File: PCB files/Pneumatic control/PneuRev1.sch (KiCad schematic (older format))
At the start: 52 parts, among them J1 SIG_IN, J2 BATT_IN, J3 PNEU, U1 uA7824, U2 OP279, U3 OP279, U4 OP279, U5 OP279, U6 OP279, U7 OP279, U8 OP07

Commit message: 2/4/2019
-Finished board routing
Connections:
- net at U1.3 (OUT), U2.8 (V+), U3.8 (V+)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: now also U2.8 (V+), U3.8 (V+), U4.8 (V+), U4.8 (V+), U5.8 (V+), U6.8 (V+), U7.8 (V+), U7.8 (V+)
- no-connect marks 24 -> 22
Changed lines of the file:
@@
 EESchema Schematic File Version 2
+LIBS:PneuRev1-rescue
 LIBS:power
 LIBS:device
@@
 	1    0    0    -1
 $EndComp
-NoConn ~ 4625 1800
-NoConn ~ 4725 1800
 Wire Wire Line
 	4925 1500 5325 1500
@@
 	1950 875  1900 875
 $Comp
-L GND #PWR?
+L GND #PWR041
 U 1 1 5C53AC5E
 P 2350 1100
-F 0 "#PWR?" H 2350 850 50  0001 C CNN
+F 0 "#PWR041" H 2350 850 50  0001 C CNN
 F 1 "GND" H 2350 950 50  0000 C CNN
 F 2 "" H 2350 1100 50  0001 C CNN
@@
 $EndComp
 Connection ~ 2350 1025
+Wire Wire Line
+	3675 1200 3675 4325
+Connection ~ 3675 1200
+Connection ~ 3675 2775
+Connection ~ 3675 4325
 $EndSCHEMATC

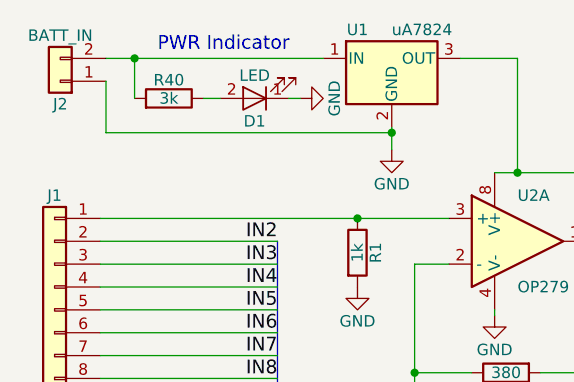
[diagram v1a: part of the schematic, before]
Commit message: 2/10/2019
-Changed LED resistor to 1.5k
-Set BATT connector to a JST
-Found 383 ohm resistor to replace 390 ohm
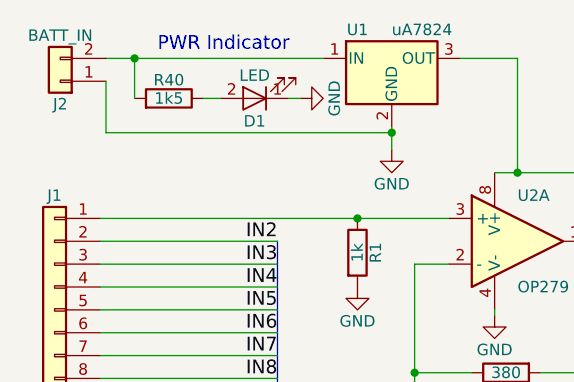
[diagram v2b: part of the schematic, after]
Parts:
- J2: footprint Connectors_Molex:Molex_KK-6410-02_02x2.54mm_Straight -> Connectors_JST:JST_XH_B02B-XH-A_02x2.50mm_Straight
- R40: value 3k -> 1k5; footprint Resistors_THT:R_Axial_DIN0204_L3.6mm_D1.6mm_P5.08mm_Horizontal -> Resistors_THT:R_Axial_DIN0411_L9.9mm_D3.6mm_P15.24mm_Horizontal
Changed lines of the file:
@@
 F 0 "J2" H 900 900 50  0000 C CNN
 F 1 "BATT_IN" H 900 600 50  0000 C CNN
-F 2 "Connectors_Molex:Molex_KK-6410-02_02x2.54mm_Straight" H 900 800 50  0001 C CNN
+F 2 "Connectors_JST:JST_XH_B02B-XH-A_02x2.50mm_Straight" H 900 800 50  0001 C CNN
 F 3 "" H 900 800 50  0001 C CNN
 	1    900  800
@@
 P 1375 875
 F 0 "R40" V 1455 875 50  0000 C CNN
-F 1 "3k" V 1375 875 50  0000 C CNN
-F 2 "Resistors_THT:R_Axial_DIN0204_L3.6mm_D1.6mm_P5.08mm_Horizontal" V 1305 875 50  0001 C CNN
+F 1 "1k5" V 1375 875 50  0000 C CNN
+F 2 "Resistors_THT:R_Axial_DIN0411_L9.9mm_D3.6mm_P15.24mm_Horizontal" V 1305 875 50  0001 C CNN
 F 3 "" H 1375 875 50  0001 C CNN
 	1    1375 875

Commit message: 2/12/2019
-Footprint updates
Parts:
- R13, R14, R15, R22, R23, R24, R31, R32, R33, R38, R4, R5, R6: footprint Resistors_THT:R_Axial_DIN0204_L3.6mm_D1.6mm_P5.08mm_Horizontal -> Resistors_THT:R_Axial_DIN0204_L3.6mm_D1.6mm_P7.62mm_Horizontal
- R16, R17, R18, R25, R26, R27, R34, R35, R36, R39: value 380 -> 400; footprint Resistors_THT:R_Axial_DIN0204_L3.6mm_D1.6mm_P5.08mm_Horizontal -> Resistors_THT:R_Axial_DIN0411_L9.9mm_D3.6mm_P12.70mm_Horizontal
- R7, R8, R9: value 380 -> 400; footprint Resistors_THT:R_Axial_DIN0204_L3.6mm_D1.6mm_P5.08mm_Horizontal -> Resistors_THT:R_Axial_DIN0309_L9.0mm_D3.2mm_P12.70mm_Horizontal
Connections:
- no-connect marks 22 -> 14
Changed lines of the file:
@@
 F 0 "R4" V 2530 2300 50  0000 C CNN
 F 1 "100" V 2450 2300 50  0000 C CNN
-F 2 "Resistors_THT:R_Axial_DIN0204_L3.6mm_D1.6mm_P5.08mm_Horizontal" V 2380 2300 50  0001 C CNN
+F 2 "Resistors_THT:R_Axial_DIN0204_L3.6mm_D1.6mm_P7.62mm_Horizontal" V 2400 2300 50  0001 C CNN
 F 3 "" H 2450 2300 50  0001 C CNN
 	1    2450 2300
@@
 P 2850 2075
 F 0 "R7" V 2930 2075 50  0000 C CNN
-F 1 "380" V 2850 2075 50  0000 C CNN
-F 2 "Resistors_THT:R_Axial_DIN0204_L3.6mm_D1.6mm_P5.08mm_Horizontal" V 2780 2075 50  0001 C CNN
+F 1 "400" V 2850 2075 50  0000 C CNN
+F 2 "Resistors_THT:R_Axial_DIN0309_L9.0mm_D3.2mm_P12.70mm_Horizontal" V 2780 2075 50  0001 C CNN
 F 3 "" H 2850 2075 50  0001 C CNN
 	1    2850 2075
@@
 F 0 "R5" V 2530 3875 50  0000 C CNN
 F 1 "100" V 2450 3875 50  0000 C CNN
-F 2 "Resistors_THT:R_Axial_DIN0204_L3.6mm_D1.6mm_P5.08mm_Horizontal" V 2380 3875 50  0001 C CNN
+F 2 "Resistors_THT:R_Axial_DIN0204_L3.6mm_D1.6mm_P7.62mm_Horizontal" V 2400 3875 50  0001 C CNN
 F 3 "" H 2450 3875 50  0001 C CNN
 	1    2450 3875
@@
 P 2850 3650
 F 0 "R8" V 2930 3650 50  0000 C CNN
-F 1 "380" V 2850 3650 50  0000 C CNN
-F 2 "Resistors_THT:R_Axial_DIN0204_L3.6mm_D1.6mm_P5.08mm_Horizontal" V 2780 3650 50  0001 C CNN
+F 1 "400" V 2850 3650 50  0000 C CNN
+F 2 "Resistors_THT:R_Axial_DIN0309_L9.0mm_D3.2mm_P12.70mm_Horizontal" V 2780 3650 50  0001 C CNN
 F 3 "" H 2850 3650 50  0001 C CNN
 	1    2850 3650
@@
 F 0 "R6" V 2580 5425 50  0000 C CNN
 F 1 "100" V 2500 5425 50  0000 C CNN
-F 2 "Resistors_THT:R_Axial_DIN0204_L3.6mm_D1.6mm_P5.08mm_Horizontal" V 2430 5425 50  0001 C CNN
+F 2 "Resistors_THT:R_Axial_DIN0204_L3.6mm_D1.6mm_P7.62mm_Horizontal" V 2430 5425 50  0001 C CNN
 F 3 "" H 2500 5425 50  0001 C CNN
 	1    2500 5425
@@
 P 2900 5200
 F 0 "R9" V 2980 5200 50  0000 C CNN
-F 1 "380" V 2900 5200 50  0000 C CNN
-F 2 "Resistors_THT:R_Axial_DIN0204_L3.6mm_D1.6mm_P5.08mm_Horizontal" V 2830 5200 50  0001 C CNN
+F 1 "400" V 2900 5200 50  0000 C CNN
+F 2 "Resistors_THT:R_Axial_DIN0309_L9.0mm_D3.2mm_P12.70mm_Horizontal" V 2830 5200 50  0001 C CNN
 F 3 "" H 2900 5200 50  0001 C CNN
 	1    2900 5200
@@
 F 0 "R13" V 4255 2300 50  0000 C CNN
 F 1 "100" V 4175 2300 50  0000 C CNN
-F 2 "Resistors_THT:R_Axial_DIN0204_L3.6mm_D1.6mm_P5.08mm_Horizontal" V 4105 2300 50  0001 C CNN
+F 2 "Resistors_THT:R_Axial_DIN0204_L3.6mm_D1.6mm_P7.62mm_Horizontal" V 4105 2300 50  0001 C CNN
 F 3 "" H 4175 2300 50  0001 C CNN
 	1    4175 2300
@@
 P 4575 2075
 F 0 "R16" V 4655 2075 50  0000 C CNN
-F 1 "380" V 4575 2075 50  0000 C CNN
-F 2 "Resistors_THT:R_Axial_DIN0204_L3.6mm_D1.6mm_P5.08mm_Horizontal" V 4505 2075 50  0001 C CNN
+F 1 "400" V 4575 2075 50  0000 C CNN
+F 2 "Resistors_THT:R_Axial_DIN0411_L9.9mm_D3.6mm_P12.70mm_Horizontal" V 4505 2075 50  0001 C CNN
 F 3 "" H 4575 2075 50  0001 C CNN
 	1    4575 2075
@@
 F 0 "R14" V 4255 3875 50  0000 C CNN
 F 1 "100" V 4175 3875 50  0000 C CNN
-F 2 "Resistors_THT:R_Axial_DIN0204_L3.6mm_D1.6mm_P5.08mm_Horizontal" V 4105 3875 50  0001 C CNN
+F 2 "Resistors_THT:R_Axial_DIN0204_L3.6mm_D1.6mm_P7.62mm_Horizontal" V 4105 3875 50  0001 C CNN
 F 3 "" H 4175 3875 50  0001 C CNN
 	1    4175 3875
@@
 P 4575 3650
 F 0 "R17" V 4655 3650 50  0000 C CNN
-F 1 "380" V 4575 3650 50  0000 C CNN
-F 2 "Resistors_THT:R_Axial_DIN0204_L3.6mm_D1.6mm_P5.08mm_Horizontal" V 4505 3650 50  0001 C CNN
+F 1 "400" V 4575 3650 50  0000 C CNN
+F 2 "Resistors_THT:R_Axial_DIN0411_L9.9mm_D3.6mm_P12.70mm_Horizontal" V 4505 3650 50  0001 C CNN
 F 3 "" H 4575 3650 50  0001 C CNN
 	1    4575 3650
@@
 F 0 "R15" V 4305 5425 50  0000 C CNN
 F 1 "100" V 4225 5425 50  0000 C CNN
-F 2 "Resistors_THT:R_Axial_DIN0204_L3.6mm_D1.6mm_P5.08mm_Horizontal" V 4155 5425 50  0001 C CNN
+F 2 "Resistors_THT:R_Axial_DIN0204_L3.6mm_D1.6mm_P7.62mm_Horizontal" V 4155 5425 50  0001 C CNN
 F 3 "" H 4225 5425 50  0001 C CNN
 	1    4225 5425
@@
 P 4625 5200
 F 0 "R18" V 4705 5200 50  0000 C CNN
-F 1 "380" V 4625 5200 50  0000 C CNN
-F 2 "Resistors_THT:R_Axial_DIN0204_L3.6mm_D1.6mm_P5.08mm_Horizontal" V 4555 5200 50  0001 C CNN
+F 1 "400" V 4625 5200 50  0000 C CNN
+F 2 "Resistors_THT:R_Axial_DIN0411_L9.9mm_D3.6mm_P12.70mm_Horizontal" V 4555 5200 50  0001 C CNN
 F 3 "" H 4625 5200 50  0001 C CNN
 	1    4625 5200
@@
 F 0 "R22" V 5830 2300 50  0000 C CNN
 F 1 "100" V 5750 2300 50  0000 C CNN
-F 2 "Resistors_THT:R_Axial_DIN0204_L3.6mm_D1.6mm_P5.08mm_Horizontal" V 5680 2300 50  0001 C CNN
+F 2 "Resistors_THT:R_Axial_DIN0204_L3.6mm_D1.6mm_P7.62mm_Horizontal" V 5680 2300 50  0001 C CNN
 F 3 "" H 5750 2300 50  0001 C CNN
 	1    5750 2300
@@
 P 6150 2075
 F 0 "R25" V 6230 2075 50  0000 C CNN
-F 1 "380" V 6150 2075 50  0000 C CNN
-F 2 "Resistors_THT:R_Axial_DIN0204_L3.6mm_D1.6mm_P5.08mm_Horizontal" V 6080 2075 50  0001 C CNN
+F 1 "400" V 6150 2075 50  0000 C CNN
+F 2 "Resistors_THT:R_Axial_DIN0411_L9.9mm_D3.6mm_P12.70mm_Horizontal" V 6080 2075 50  0001 C CNN
 F 3 "" H 6150 2075 50  0001 C CNN
 	1    6150 2075
@@
 	1    0    0    -1
 $EndComp
-NoConn ~ 6200 1800
-NoConn ~ 6300 1800
 Wire Wire Line
 	6500 1500 7000 1500
@@
 F 0 "R23" V 5830 3875 50  0000 C CNN
 F 1 "100" V 5750 3875 50  0000 C CNN
-F 2 "Resistors_THT:R_Axial_DIN0204_L3.6mm_D1.6mm_P5.08mm_Horizontal" V 5680 3875 50  0001 C CNN
+F 2 "Resistors_THT:R_Axial_DIN0204_L3.6mm_D1.6mm_P7.62mm_Horizontal" V 5680 3875 50  0001 C CNN
 F 3 "" H 5750 3875 50  0001 C CNN
 	1    5750 3875
@@
 P 6150 3650
 F 0 "R26" V 6230 3650 50  0000 C CNN
-F 1 "380" V 6150 3650 50  0000 C CNN
-F 2 "Resistors_THT:R_Axial_DIN0204_L3.6mm_D1.6mm_P5.08mm_Horizontal" V 6080 3650 50  0001 C CNN
+F 1 "400" V 6150 3650 50  0000 C CNN
+F 2 "Resistors_THT:R_Axial_DIN0411_L9.9mm_D3.6mm_P12.70mm_Horizontal" V 6080 3650 50  0001 C CNN
 F 3 "" H 6150 3650 50  0001 C CNN
 	1    6150 3650
@@
 	1    0    0    -1
 $EndComp
-NoConn ~ 6200 3375
-NoConn ~ 6300 3375
 Wire Wire Line
 	6500 3075 7000 3075
@@
 F 0 "R24" V 5880 5425 50  0000 C CNN
 F 1 "100" V 5800 5425 50  0000 C CNN
-F 2 "Resistors_THT:R_Axial_DIN0204_L3.6mm_D1.6mm_P5.08mm_Horizontal" V 5730 5425 50  0001 C CNN
+F 2 "Resistors_THT:R_Axial_DIN0204_L3.6mm_D1.6mm_P7.62mm_Horizontal" V 5730 5425 50  0001 C CNN
 F 3 "" H 5800 5425 50  0001 C CNN
 	1    5800 5425
@@
 P 6200 5200
 F 0 "R27" V 6280 5200 50  0000 C CNN
-F 1 "380" V 6200 5200 50  0000 C CNN
-F 2 "Resistors_THT:R_Axial_DIN0204_L3.6mm_D1.6mm_P5.08mm_Horizontal" V 6130 5200 50  0001 C CNN
+F 1 "400" V 6200 5200 50  0000 C CNN
+F 2 "Resistors_THT:R_Axial_DIN0411_L9.9mm_D3.6mm_P12.70mm_Horizontal" V 6130 5200 50  0001 C CNN
 F 3 "" H 6200 5200 50  0001 C CNN
 	1    6200 5200
@@
 F 0 "R31" V 7580 2300 50  0000 C CNN
 F 1 "100" V 7500 2300 50  0000 C CNN
-F 2 "Resistors_THT:R_Axial_DIN0204_L3.6mm_D1.6mm_P5.08mm_Horizontal" V 7430 2300 50  0001 C CNN
+F 2 "Resistors_THT:R_Axial_DIN0204_L3.6mm_D1.6mm_P7.62mm_Horizontal" V 7430 2300 50  0001 C CNN
 F 3 "" H 7500 2300 50  0001 C CNN
 	1    7500 2300
@@
 P 7900 2075
 F 0 "R34" V 7980 2075 50  0000 C CNN
-F 1 "380" V 7900 2075 50  0000 C CNN
-F 2 "Resistors_THT:R_Axial_DIN0204_L3.6mm_D1.6mm_P5.08mm_Horizontal" V 7830 2075 50  0001 C CNN
+F 1 "400" V 7900 2075 50  0000 C CNN
+F 2 "Resistors_THT:R_Axial_DIN0411_L9.9mm_D3.6mm_P12.70mm_Horizontal" V 7830 2075 50  0001 C CNN
 F 3 "" H 7900 2075 50  0001 C CNN
 	1    7900 2075
@@
 	1    0    0    -1
 $EndComp
-NoConn ~ 7950 1800
-NoConn ~ 8050 1800
 Wire Wire Line
 	8250 1500 8675 1500
@@
 F 0 "R32" V 7580 3875 50  0000 C CNN
 F 1 "100" V 7500 3875 50  0000 C CNN
-F 2 "Resistors_THT:R_Axial_DIN0204_L3.6mm_D1.6mm_P5.08mm_Horizontal" V 7430 3875 50  0001 C CNN
+F 2 "Resistors_THT:R_Axial_DIN0204_L3.6mm_D1.6mm_P7.62mm_Horizontal" V 7430 3875 50  0001 C CNN
 F 3 "" H 7500 3875 50  0001 C CNN
 	1    7500 3875
@@
 P 7900 3650
 F 0 "R35" V 7980 3650 50  0000 C CNN
-F 1 "380" V 7900 3650 50  0000 C CNN
-F 2 "Resistors_THT:R_Axial_DIN0204_L3.6mm_D1.6mm_P5.08mm_Horizontal" V 7830 3650 50  0001 C CNN
+F 1 "400" V 7900 3650 50  0000 C CNN
+F 2 "Resistors_THT:R_Axial_DIN0411_L9.9mm_D3.6mm_P12.70mm_Horizontal" V 7830 3650 50  0001 C CNN
 F 3 "" H 7900 3650 50  0001 C CNN
 	1    7900 3650
@@
 	1    0    0    -1
 $EndComp
-NoConn ~ 7950 3375
-NoConn ~ 8050 3375
 Wire Wire Line
 	8250 3075 8675 3075
@@
 U 1 1 5C023441
 P 7300 4675
-F 0 "R30" V 7380 4675 50  0000 C CNN
+F 0 "R30" V 7400 4675 50  0000 C CNN
 F 1 "1k" V 7300 4675 50  0000 C CNN
 F 2 "Resistors_THT:R_Axial_DIN0204_L3.6mm_D1.6mm_P5.08mm_Horizontal" V 7230 4675 50  0001 C CNN
@@
 F 0 "R33" V 7630 5425 50  0000 C CNN
 F 1 "100" V 7550 5425 50  0000 C CNN
-F 2 "Resistors_THT:R_Axial_DIN0204_L3.6mm_D1.6mm_P5.08mm_Horizontal" V 7480 5425 50  0001 C CNN
+F 2 "Resistors_THT:R_Axial_DIN0204_L3.6mm_D1.6mm_P7.62mm_Horizontal" V 7480 5425 50  0001 C CNN
 F 3 "" H 7550 5425 50  0001 C CNN
 	1    7550 5425
@@
 P 7950 5200
 F 0 "R36" V 8030 5200 50  0000 C CNN
-F 1 "380" V 7950 5200 50  0000 C CNN
-F 2 "Resistors_THT:R_Axial_DIN0204_L3.6mm_D1.6mm_P5.08mm_Horizontal" V 7880 5200 50  0001 C CNN
+F 1 "400" V 7950 5200 50  0000 C CNN
+F 2 "Resistors_THT:R_Axial_DIN0411_L9.9mm_D3.6mm_P12.70mm_Horizontal" V 7880 5200 50  0001 C CNN
 F 3 "" H 7950 5200 50  0001 C CNN
 	1    7950 5200
@@
 F 0 "R38" V 9055 2300 50  0000 C CNN
 F 1 "100" V 8975 2300 50  0000 C CNN
-F 2 "Resistors_THT:R_Axial_DIN0204_L3.6mm_D1.6mm_P5.08mm_Horizontal" V 8905 2300 50  0001 C CNN
+F 2 "Resistors_THT:R_Axial_DIN0204_L3.6mm_D1.6mm_P7.62mm_Horizontal" V 8905 2300 50  0001 C CNN
 F 3 "" H 8975 2300 50  0001 C CNN
 	1    8975 2300
@@
 P 9375 2075
 F 0 "R39" V 9455 2075 50  0000 C CNN
-F 1 "380" V 9375 2075 50  0000 C CNN
-F 2 "Resistors_THT:R_Axial_DIN0204_L3.6mm_D1.6mm_P5.08mm_Horizontal" V 9305 2075 50  0001 C CNN
+F 1 "400" V 9375 2075 50  0000 C CNN
+F 2 "Resistors_THT:R_Axial_DIN0411_L9.9mm_D3.6mm_P12.70mm_Horizontal" V 9305 2075 50  0001 C CNN
 F 3 "" H 9375 2075 50  0001 C CNN
 	1    9375 2075

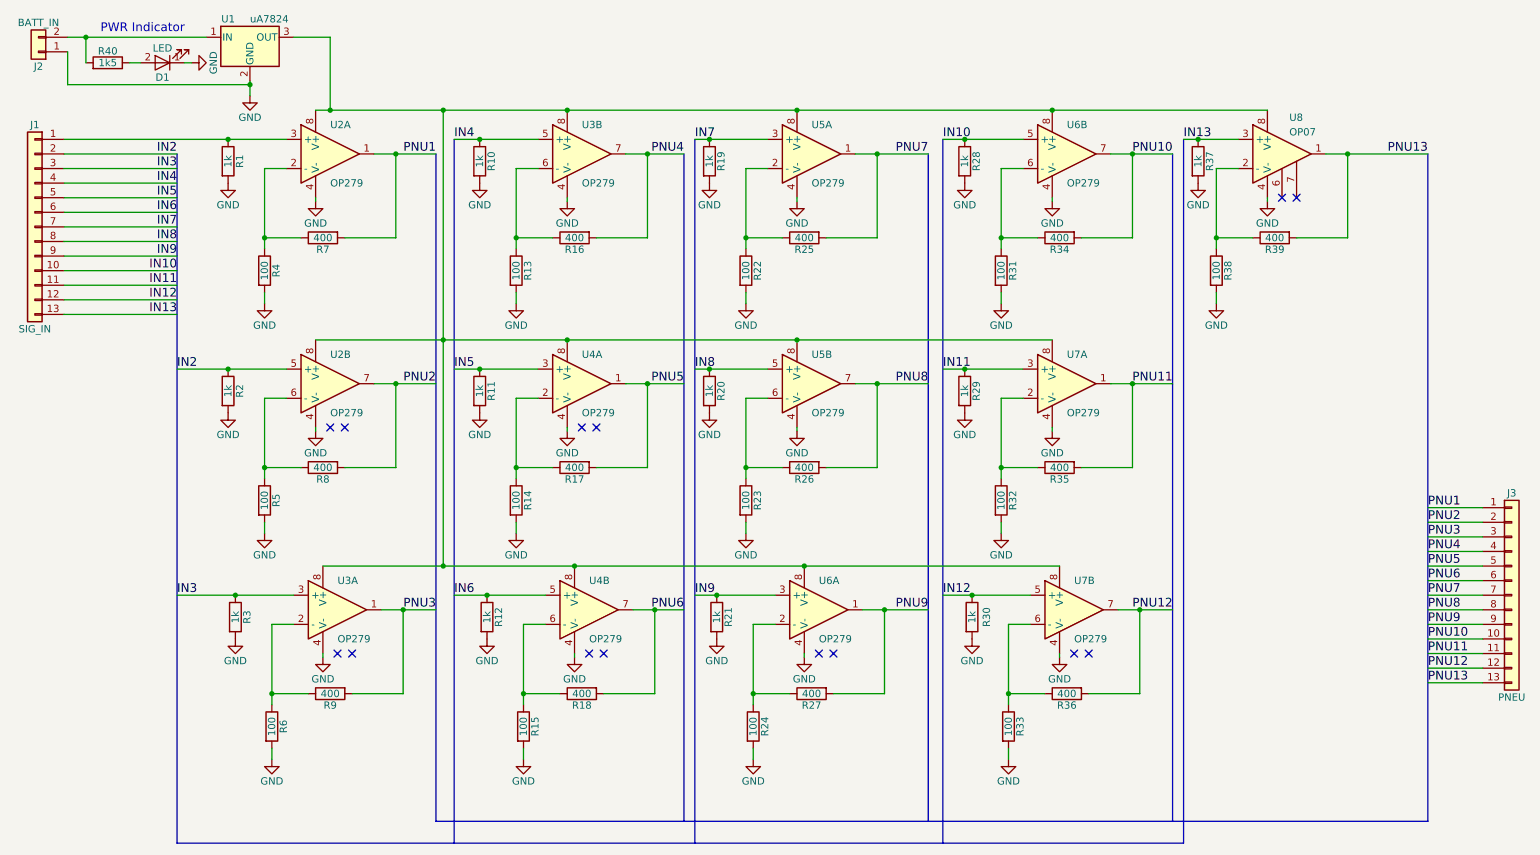
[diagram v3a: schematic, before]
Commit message: 2/15/2019
-Created symbol for OPA551
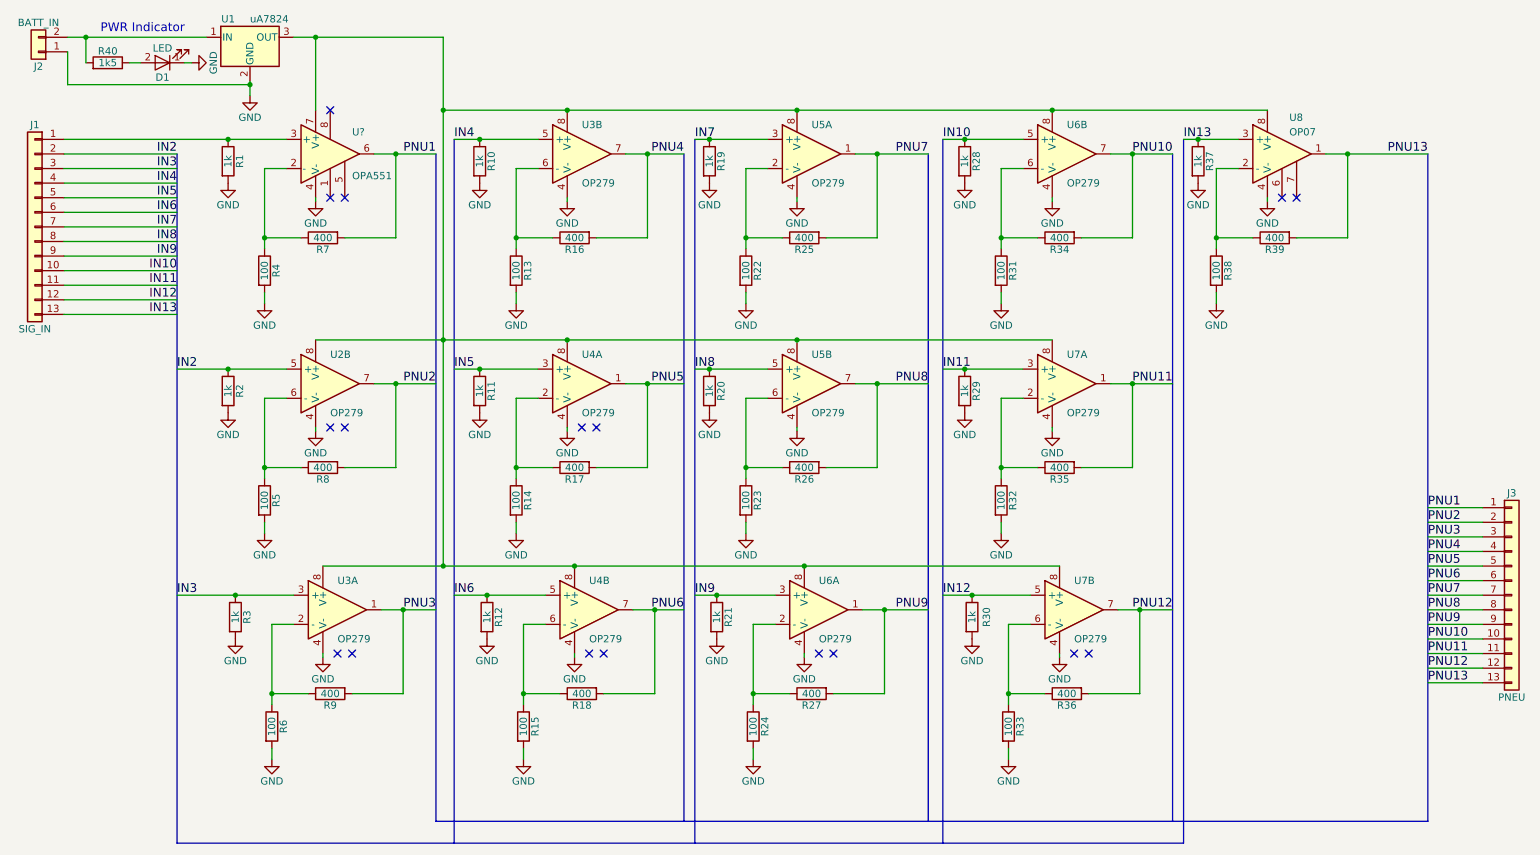
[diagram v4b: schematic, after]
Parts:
- removed unit 1 of U2
- added U?: OPA551, symbol OPA551
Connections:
- net GND: now also U?.4 (V-)
- net PNU1: now also U?.6
- net at J1.1 (Pin_1), R1.1: now also U?.3 (+)
- net at R4.1, R7.1: now also U?.2 (-)
- net at U1.3 (OUT), U2.8 (V+), U3.8 (V+)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: now also U?.7 (V+)
- no-connect marks 14 -> 17
